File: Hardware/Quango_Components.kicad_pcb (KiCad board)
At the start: 2 copper layers, 80.7 x 100 mm, 148 parts, among them J1 Conn_01x12_Male, J2 Conn_01x12_Male, J3 Conn_01x12_Male, J4 Conn_01x12_Male, J5 SWD_Header, J6 Eurorack_10_pin_power, Q1 MMBT3904, U1 LM1117-3.3, U10 TL074, U11 TL074, U12 TL074, U13 TL074, U14 TL074, U2 STM32G473V, U3 LM1117-5.0, U4 PS508, U5 MCP6002, U6 AS3364, U7 AS3364, U8 AD5676, U9 MCP48CMB21, Y1 8MHz 20pF

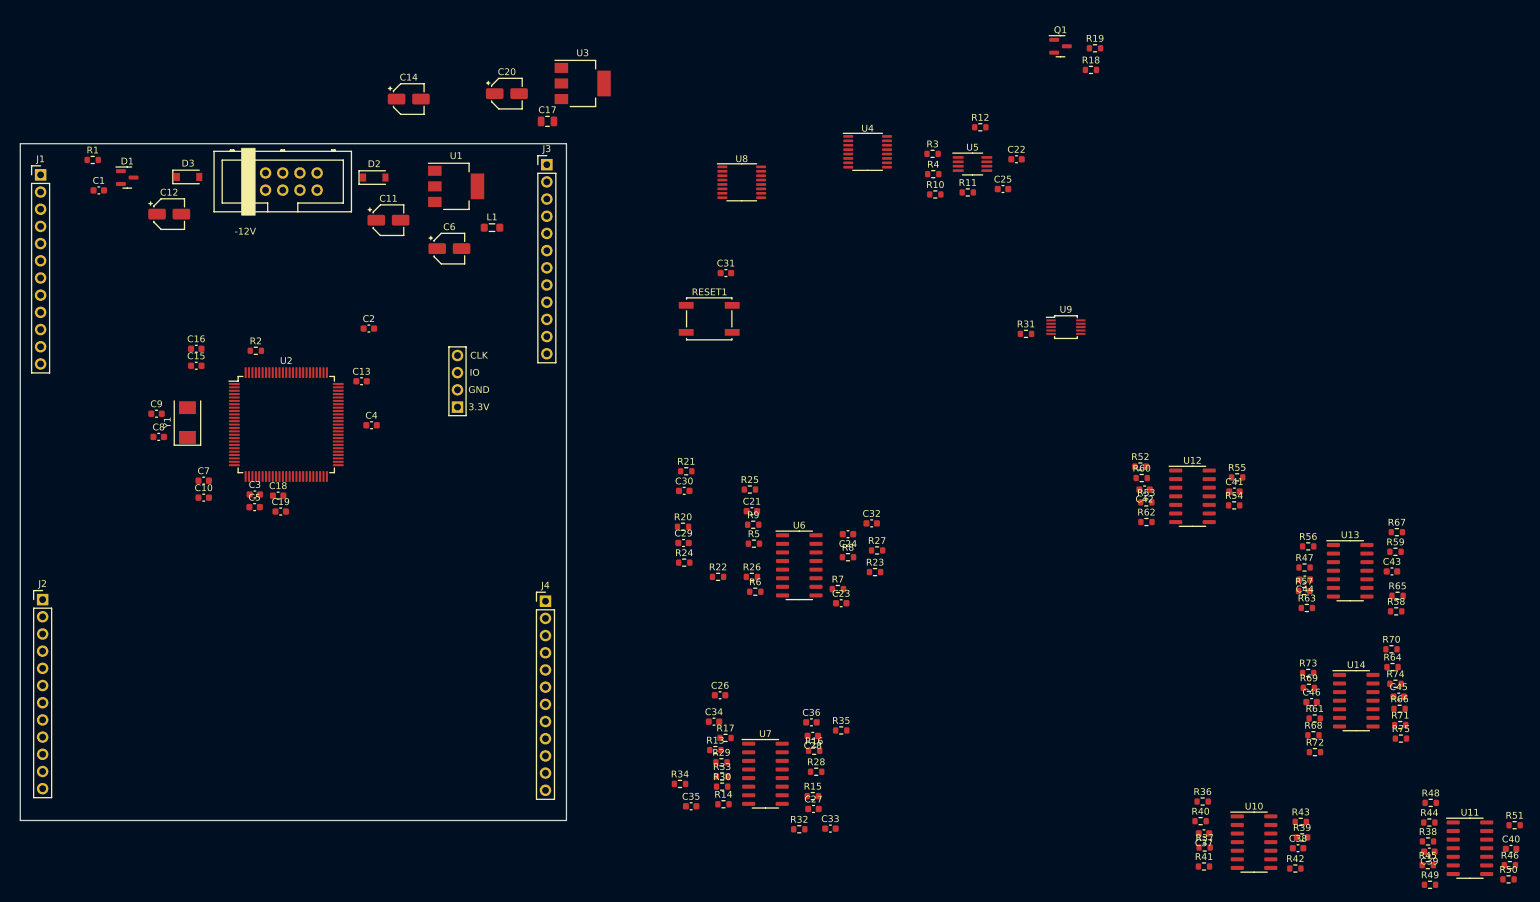
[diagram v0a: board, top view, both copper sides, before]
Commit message: Started op-amp layout
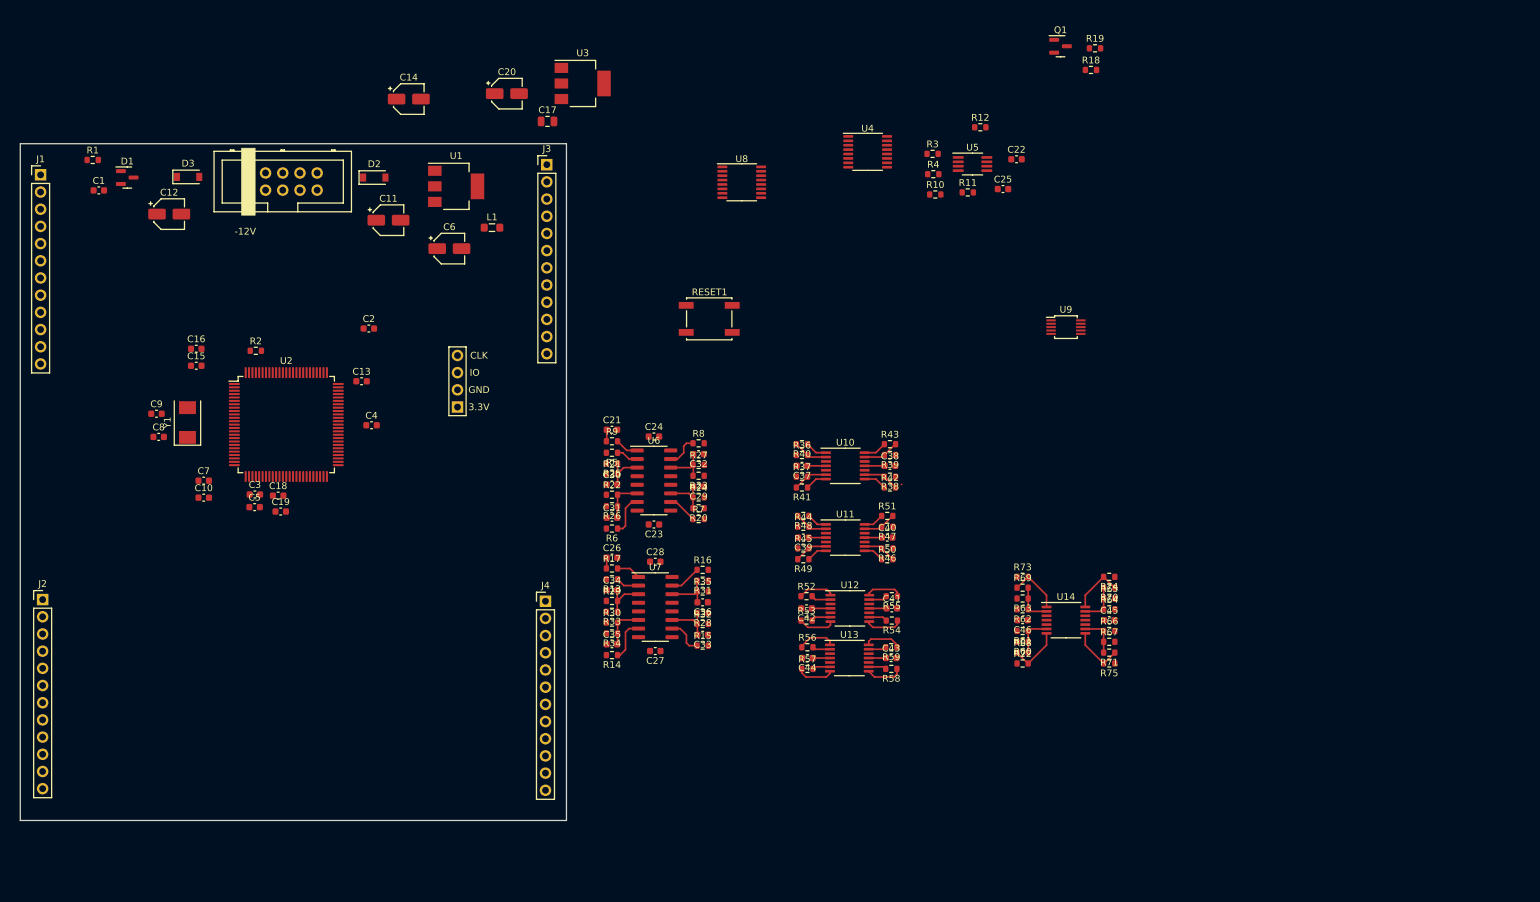
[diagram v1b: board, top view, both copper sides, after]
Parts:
- U10, U11, U12, U13, U14: footprint Package_SO:SOIC-14_3.9x8.7mm_P1.27mm -> Package_SO:TSSOP-14_4.4x5mm_P0.65mm
- moved R49 104.3 mm to (165.8, 100.4), turned to 180 degrees
- moved C39 103.5 mm to (165.8, 97.2)
- moved R45 103.5 mm to (165.8, 98.8)
- moved R51 103.4 mm to (178.2, 94.0)
- moved R50 103.3 mm to (178.2, 100.4)
- moved R46 103.2 mm to (178.2, 98.8), turned to 180 degrees
- moved U11 103.1 mm to (172.0, 97.2)
- moved C40 103.0 mm to (178.2, 97.2)
- moved R44 102.3 mm to (165.8, 95.6)
- moved R48 101.9 mm to (165.8, 94.0), turned to 180 degrees
- moved R38 96.0 mm to (178.6, 88.2), turned to 180 degrees
- moved R39 83.1 mm to (178.6, 85.0), turned to 180 degrees
- moved C38 82.6 mm to (178.6, 86.6)
- moved R43 82.5 mm to (178.6, 83.4)
- moved R42 82.2 mm to (178.6, 89.8)
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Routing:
- net -12V: track 0.00 -> 11.6 mm
- net +12V: track 0.00 -> 11.2 mm
- net Net-(R68-Pad1): track 0.00 -> 7.89 mm
- net Net-(R69-Pad1): track 0.00 -> 7.89 mm
- net Net-(R71-Pad1): track 0.00 -> 7.89 mm
- net Net-(R70-Pad1): track 0.00 -> 7.89 mm
- net /EnvB3_Scaled: track 0.00 -> 7.17 mm
- net /EnvB4_Scaled: track 0.00 -> 7.09 mm
- net /EnvA3_Scaled: track 0.00 -> 6.77 mm
- net /EnvB1_Scaled: track 0.00 -> 6.74 mm
- net /EnvA4_Scaled: track 0.00 -> 6.68 mm
- net /EnvB2_Scaled: track 0.00 -> 6.48 mm
- net /EnvA2_Scaled: track 0.00 -> 6.40 mm
- net /EnvA1_Scaled: track 0.00 -> 6.40 mm
- net Net-(R14-Pad1): track 0.00 -> 6.25 mm
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
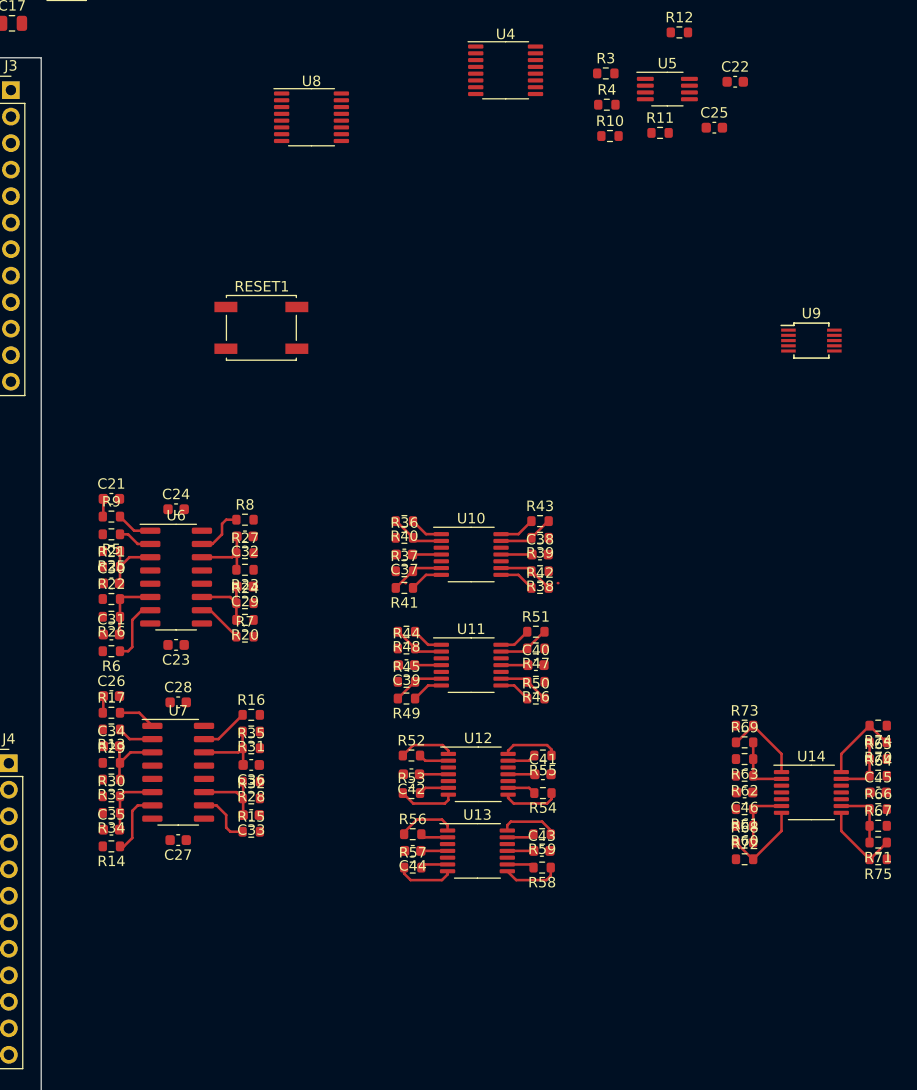
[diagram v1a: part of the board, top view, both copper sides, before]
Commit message: Layout of audio vca section
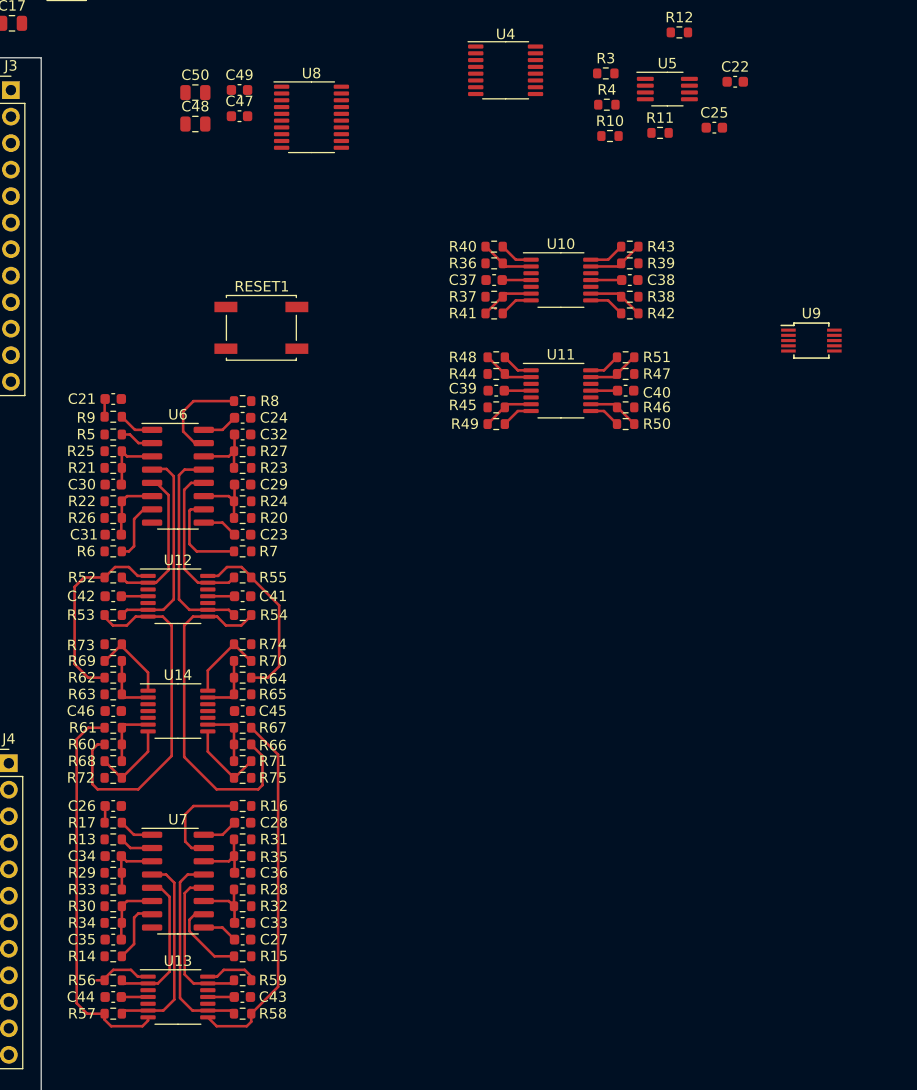
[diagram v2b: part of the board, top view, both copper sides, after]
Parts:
- added C47: 100nF, Capacitor_SMD:C_0603_1608Metric, F.Cu at (149.8, 44.6)
- added C48: 10uF, Capacitor_SMD:C_0805_2012Metric, F.Cu at (145.6, 45.4)
- added C49: 100nF, Capacitor_SMD:C_0603_1608Metric, F.Cu at (149.8, 42.1)
- added C50: 10uF, Capacitor_SMD:C_0805_2012Metric, F.Cu at (145.6, 42.3)
- U8: footprint Package_SO:TSSOP-16_4.4x5mm_P0.65mm -> Package_SO:TSSOP-20_4.4x6.5mm_P0.65mm
- moved R64 61.6 mm to (150.1, 98.4)
- moved R67 61.6 mm to (150.1, 103.2)
- moved C45 61.4 mm to (150.1, 101.6)
- moved R70 61.4 mm to (150.1, 96.8)
- moved R71 61.4 mm to (150.1, 106.4)
- moved R74 61.4 mm to (150.1, 95.2)
- moved R75 61.4 mm to (150.1, 108.0)
- moved R62 61.2 mm to (137.7, 98.4)
- moved R65 61.2 mm to (150.1, 100.0)
- moved R66 61.2 mm to (150.1, 104.8)
- moved U14 61.2 mm to (143.9, 101.6)
- moved C46 61.0 mm to (137.7, 101.6)
- moved R60 61.0 mm to (137.7, 104.8)
- moved R61 61.0 mm to (137.7, 103.2)
- moved R68 61.0 mm to (137.7, 106.4)
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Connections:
- R52 pad 1: /OpAmps/AudioA1_Out -> /OpAmps/AudioA2_Out
- R52 pad 2: /AudioB1_VCA -> /AudioA2_VCA
- R53 pad 1: /OpAmps/AudioA2_Out -> /OpAmps/AudioA1_Out
- R53 pad 2: /AudioB2_VCA -> /AudioA1_VCA
- R54 pad 1: /OpAmps/AudioA3_Out -> /OpAmps/AudioA4_Out
- R54 pad 2: /AudioB3_VCA -> /AudioA4_VCA
- R55 pad 1: /OpAmps/AudioA4_Out -> /OpAmps/AudioA3_Out
- R55 pad 2: /AudioB4_VCA -> /AudioA3_VCA
- R56 pad 1: /OpAmps/AudioB1_Out -> /OpAmps/AudioB2_Out
- R56 pad 2: /AudioA1_VCA -> /AudioB2_VCA
- R57 pad 1: /OpAmps/AudioB2_Out -> /OpAmps/AudioB1_Out
- R57 pad 2: /AudioA2_VCA -> /AudioB1_VCA
- R58 pad 1: /OpAmps/AudioB3_Out -> /OpAmps/AudioB4_Out
- R58 pad 2: /AudioA3_VCA -> /AudioB4_VCA
- R59 pad 1: /OpAmps/AudioB4_Out -> /OpAmps/AudioB3_Out
- R59 pad 2: /AudioA4_VCA -> /AudioB3_VCA
- U12 pad 1: /OpAmps/AudioA1_Out -> /OpAmps/AudioA2_Out
- U12 pad 13: /AudioB4_VCA -> /AudioA3_VCA
- U12 pad 14: /OpAmps/AudioA4_Out -> /OpAmps/AudioA3_Out
- U12 pad 2: /AudioB1_VCA -> /AudioA2_VCA
- U12 pad 6: /AudioB2_VCA -> /AudioA1_VCA
- U12 pad 7: /OpAmps/AudioA2_Out -> /OpAmps/AudioA1_Out
- U12 pad 8: /OpAmps/AudioA3_Out -> /OpAmps/AudioA4_Out
- U12 pad 9: /AudioB3_VCA -> /AudioA4_VCA
- U13 pad 1: /OpAmps/AudioB1_Out -> /OpAmps/AudioB2_Out
- U13 pad 13: /AudioA4_VCA -> /AudioB3_VCA
- U13 pad 14: /OpAmps/AudioB4_Out -> /OpAmps/AudioB3_Out
- U13 pad 2: /AudioA1_VCA -> /AudioB2_VCA
- U13 pad 6: /AudioA2_VCA -> /AudioB1_VCA
- U13 pad 7: /OpAmps/AudioB2_Out -> /OpAmps/AudioB1_Out
- U13 pad 8: /OpAmps/AudioB3_Out -> /OpAmps/AudioB4_Out
- U13 pad 9: /AudioA3_VCA -> /AudioB4_VCA
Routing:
- net /OpAmps/AudioB1_Out: track 5.58 -> 37.1 mm
- net /OpAmps/AudioB4_Out: track 5.53 -> 35.0 mm
- net /OpAmps/AudioA1_Out: track 5.31 -> 34.0 mm
- net /OpAmps/AudioA4_Out: track 5.45 -> 33.2 mm
- net /AudioA4_VCA: track 2.64 -> 20.4 mm
- net /AudioA1_VCA: track 2.64 -> 19.8 mm
- net /AudioB4_VCA: track 2.72 -> 19.5 mm
- net /AudioB1_VCA: track 2.92 -> 19.2 mm
- net /OpAmps/AudioA2_Out: track 5.43 -> 19.0 mm
- net /AudioA3_VCA: track 2.64 -> 15.3 mm
- net /AudioB3_VCA: track 2.72 -> 15.0 mm
- net /OpAmps/AudioA3_Out: track 5.45 -> 17.7 mm
- net /AudioA2_VCA: track 2.64 -> 14.4 mm
- net /AudioB2_VCA: track 2.92 -> 14.4 mm
- net +12V: track 11.2 -> 18.1 mm
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
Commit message: Further Layout
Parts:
- added C51: 100nF, Capacitor_SMD:C_0603_1608Metric, F.Cu at (64.5, 106.7)
- added C52: 10uF, Capacitor_SMD:C_0805_2012Metric, F.Cu at (64.5, 108.5)
- added C53: 100nF, Capacitor_SMD:C_0603_1608Metric, F.Cu at (64.5, 105.2)
- added C54: 10uF, Capacitor_SMD:C_0805_2012Metric, F.Cu at (64.5, 103.4)
- moved U9 140.6 mm to (70.0, 106.7)
- moved U12 74.5 mm to (70.0, 81.3)
- moved U14 74.5 mm to (70.0, 92.3)
- moved U6 74.5 mm to (70.0, 69.8)
- moved C23 74.5 mm to (76.2, 75.4)
- moved C24 74.5 mm to (76.2, 64.2)
- moved C29 74.5 mm to (76.2, 70.6)
- moved C30 74.5 mm to (63.8, 70.6)
- moved C31 74.5 mm to (63.8, 75.4)
- moved C32 74.5 mm to (76.2, 65.8)
- moved C41 74.5 mm to (76.2, 81.3)
- moved C42 74.5 mm to (63.8, 81.3)
- moved C45 74.5 mm to (76.2, 92.3)
- moved C46 74.5 mm to (63.8, 92.3)
- moved R20 74.5 mm to (76.2, 73.8)
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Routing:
- net /OpAmps/AudioB3_Out: track 5.07 -> 36.1 mm
- net /OpAmps/AudioB2_Out: track 5.72 -> 35.9 mm
- net /OpAmps/AudioB4_Out: track 35.0 -> 35.9 mm
